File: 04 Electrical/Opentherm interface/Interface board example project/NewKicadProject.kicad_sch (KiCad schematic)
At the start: 17 parts, among them J1 Boiler, J2 Screw_Terminal_01x04, Q1 BC858, U1 EL357N(C)(TA)-G, U2 EL357N(C)(TA)-G

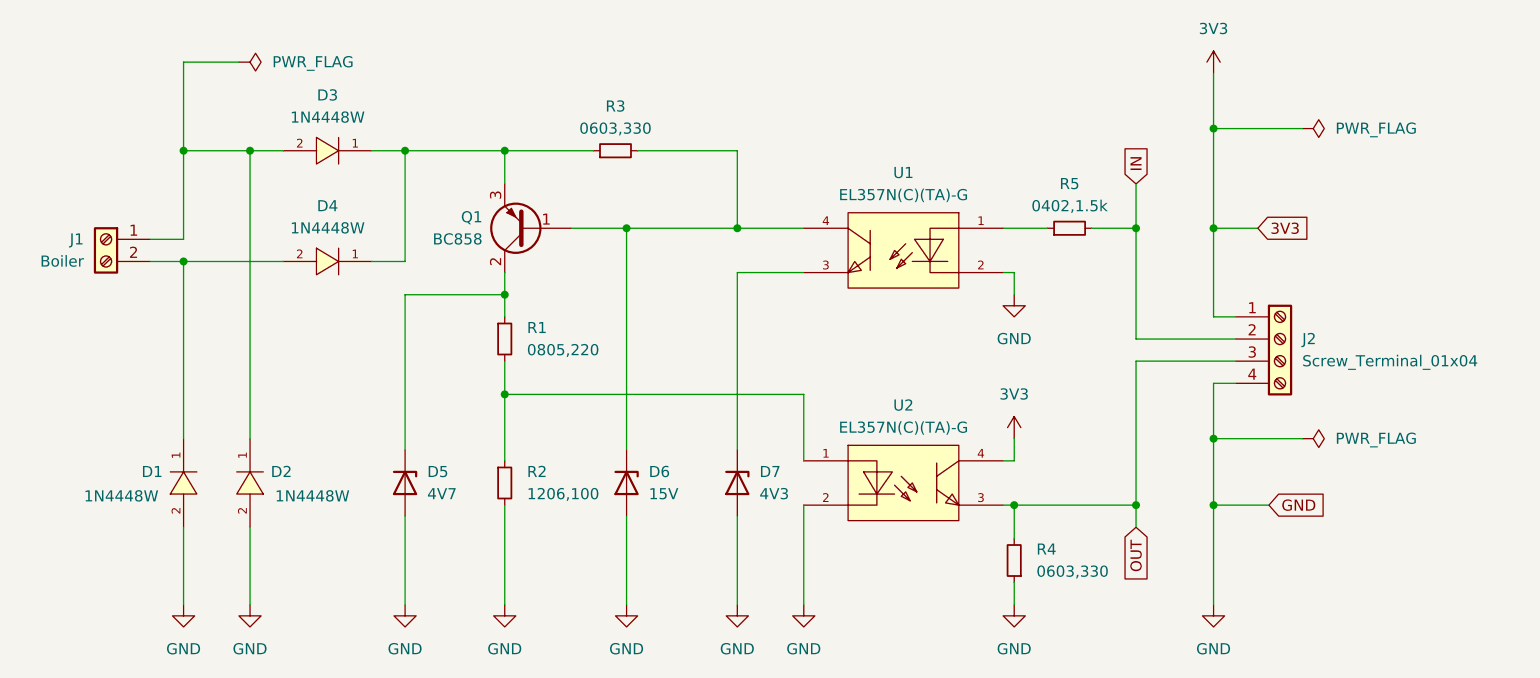
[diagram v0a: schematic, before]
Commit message: Reverse engineering OpenTherm
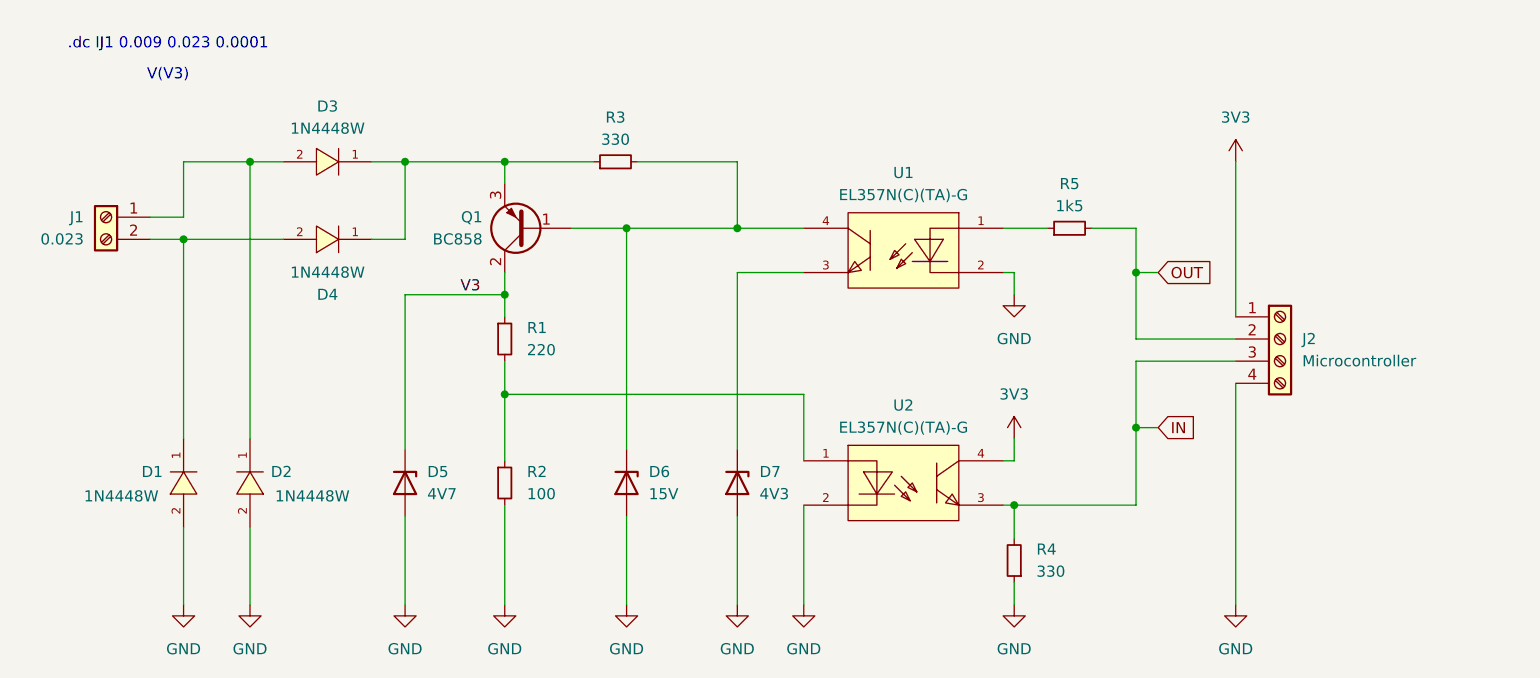
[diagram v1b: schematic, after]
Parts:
- J1: value Boiler -> 0.023
- J2: value Screw_Terminal_01x04 -> Microcontroller
- R1: value 0805,220 -> 220
- R2: value 1206,100 -> 100
- R3, R4: value 0603,330 -> 330
- R5: value 0402,1.5k -> 1k5
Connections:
- net IN: now also J2.3 (Pin_3), R4.2, U2.3 (EM); no longer J2.2 (Pin_2), R5.2
- net OUT: now also J2.2 (Pin_2), R5.2; no longer J2.3 (Pin_3), R4.2, U2.3 (EM)
- net V3: now reaches D5.1 (K), Q1.2 (C), R1.1
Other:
- note added: ".dc IJ1 0.009 0.023 0.0001"
- note added: "V(V3)"
- moved on the sheet: D3, D4, J1, R3
